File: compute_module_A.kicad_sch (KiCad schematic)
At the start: 15 parts, among them J6 MagJack, J7 Micro_SD_Card_Det, U4 RT9742GGJ5

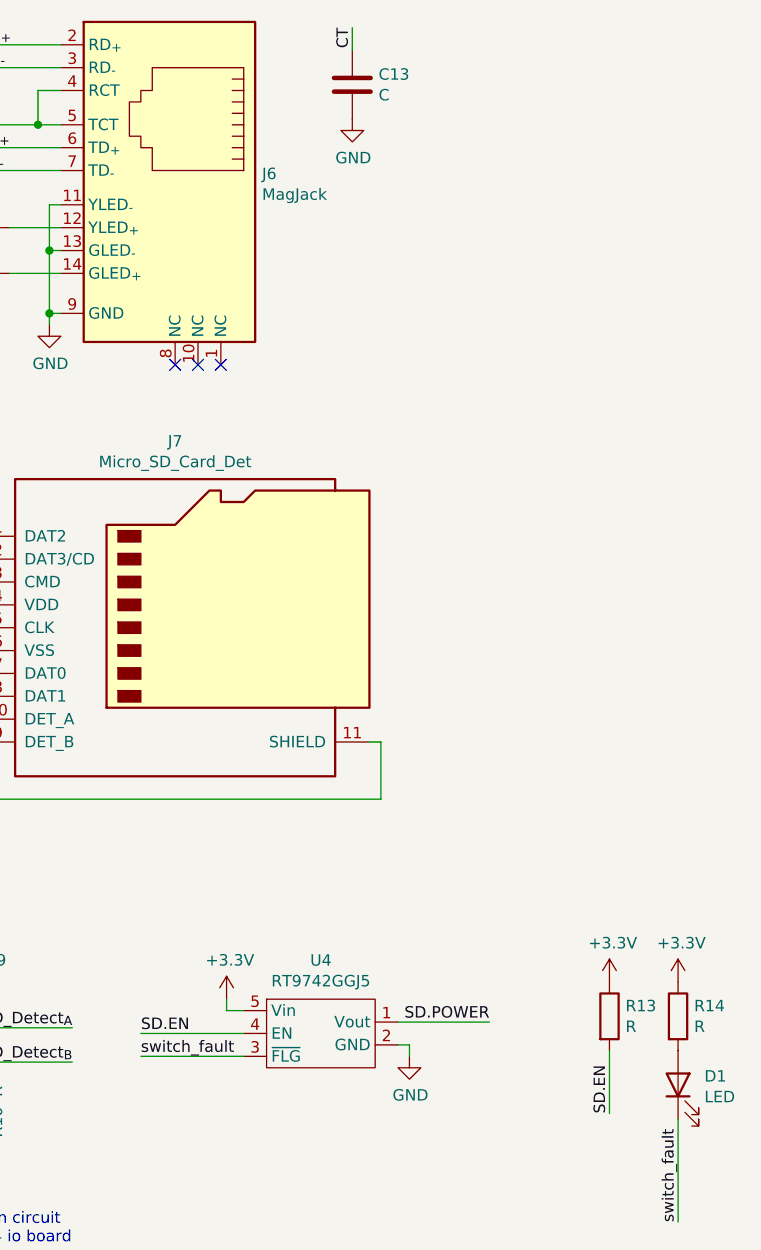
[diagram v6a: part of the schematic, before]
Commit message: footprint assignments
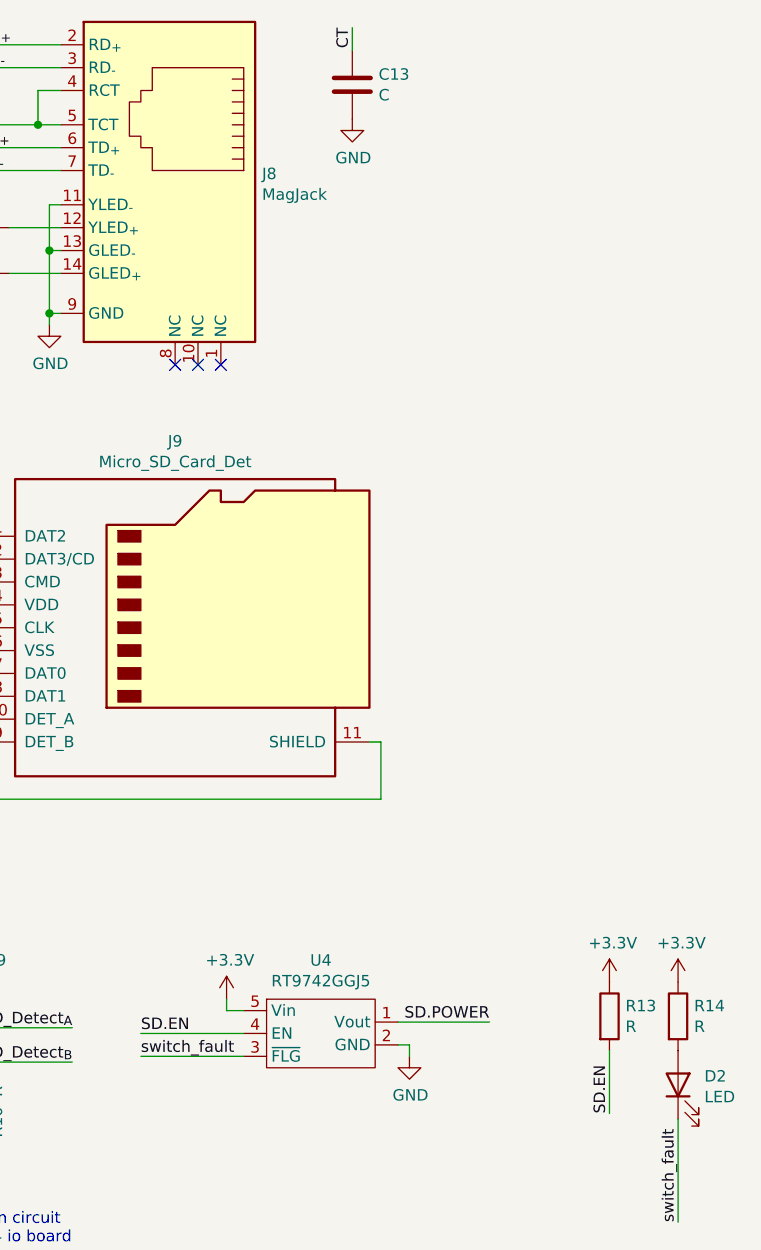
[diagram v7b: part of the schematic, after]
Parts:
- J9: renamed from J7; Vendor Part (none) -> HR1941CT-ND
- renumbered D1 to D2, J6 to J8
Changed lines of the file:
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@@
   (junction (at 184.785 53.975) (diameter 0.9144) (color 0 0 0 0))
   (junction (at 184.785 60.96) (diameter 0.9144) (color 0 0 0 0))
+  (no_connect (at 198.755 66.675))
+  (no_connect (at 94.615 41.91))
   (no_connect (at 33.655 49.53))
+  (no_connect (at 203.835 66.675))
+  (no_connect (at 201.295 66.675))
+  (no_connect (at 33.655 52.07))
+  (no_connect (at 94.615 62.23))
   (no_connect (at 94.615 44.45))
-  (no_connect (at 198.755 66.675))
-  (no_connect (at 94.615 62.23))
-  (no_connect (at 33.655 52.07))
-  (no_connect (at 94.615 41.91))
-  (no_connect (at 201.295 66.675))
-  (no_connect (at 203.835 66.675))
   (wire (pts (xy 20.955 133.35) (xy 33.655 133.35))
     (stroke (width 0) (type solid) (color 0 0 0 0))
@@
   (symbol (lib_id "power:+3.3V") (at 28.575 125.095 0) (unit 1)
     (in_bom yes) (on_board yes)
-    (property "Reference" "#PWR0120" (id 0) (at 28.575 128.905 0)
+    (property "Reference" "#PWR0124" (id 0) (at 28.575 128.905 0)
       (effects (font (size 1.27 1.27)) hide)
     )
@@
   (symbol (lib_id "power:+5V") (at 110.49 133.985 0) (unit 1)
     (in_bom yes) (on_board yes)
-    (property "Reference" "#PWR0121" (id 0) (at 110.49 137.795 0)
+    (property "Reference" "#PWR0126" (id 0) (at 110.49 137.795 0)
       (effects (font (size 1.27 1.27)) hide)
     )
@@
   (symbol (lib_id "power:+3.3V") (at 121.92 180.975 0) (unit 1)
     (in_bom yes) (on_board yes)
-    (property "Reference" "#PWR0127" (id 0) (at 121.92 184.785 0)
+    (property "Reference" "#PWR0131" (id 0) (at 121.92 184.785 0)
       (effects (font (size 1.27 1.27)) hide)
     )
@@
   (symbol (lib_id "power:+3.3V") (at 139.065 180.975 0) (unit 1)
     (in_bom yes) (on_board yes)
-    (property "Reference" "#PWR0124" (id 0) (at 139.065 184.785 0)
+    (property "Reference" "#PWR0129" (id 0) (at 139.065 184.785 0)
       (effects (font (size 1.27 1.27)) hide)
     )
@@
   (symbol (lib_id "power:+3.3V") (at 175.895 130.175 0) (unit 1)
     (in_bom yes) (on_board yes)
-    (property "Reference" "#PWR0130" (id 0) (at 175.895 133.985 0)
+    (property "Reference" "#PWR0133" (id 0) (at 175.895 133.985 0)
       (effects (font (size 1.27 1.27)) hide)
     )
@@
   (symbol (lib_id "power:+3.3V") (at 204.47 137.16 0) (unit 1)
     (in_bom yes) (on_board yes)
-    (property "Reference" "#PWR0132" (id 0) (at 204.47 140.97 0)
+    (property "Reference" "#PWR0137" (id 0) (at 204.47 140.97 0)
       (effects (font (size 1.27 1.27)) hide)
     )
@@
   (symbol (lib_id "power:+3.3V") (at 247.015 135.255 0) (unit 1)
     (in_bom yes) (on_board yes)
-    (property "Reference" "#PWR0135" (id 0) (at 247.015 139.065 0)
+    (property "Reference" "#PWR0139" (id 0) (at 247.015 139.065 0)
       (effects (font (size 1.27 1.27)) hide)
     )
@@
   (symbol (lib_id "power:+3.3V") (at 254.635 135.255 0) (unit 1)
     (in_bom yes) (on_board yes)
-    (property "Reference" "#PWR0134" (id 0) (at 254.635 139.065 0)
+    (property "Reference" "#PWR0138" (id 0) (at 254.635 139.065 0)
       (effects (font (size 1.27 1.27)) hide)
     )
@@
   (symbol (lib_id "power:GND") (at 98.425 171.45 0) (unit 1)
     (in_bom yes) (on_board yes)
-    (property "Reference" "#PWR0126" (id 0) (at 98.425 177.8 0)
+    (property "Reference" "#PWR0125" (id 0) (at 98.425 177.8 0)
       (effects (font (size 1.27 1.27)) hide)
     )
@@
   (symbol (lib_id "power:GND") (at 121.92 188.595 0) (unit 1)
     (in_bom yes) (on_board yes)
-    (property "Reference" "#PWR0125" (id 0) (at 121.92 194.945 0)
+    (property "Reference" "#PWR0130" (id 0) (at 121.92 194.945 0)
       (effects (font (size 1.27 1.27)) hide)
     )
@@
   (symbol (lib_id "power:GND") (at 130.81 188.595 0) (unit 1)
     (in_bom yes) (on_board yes)
-    (property "Reference" "#PWR0122" (id 0) (at 130.81 194.945 0)
+    (property "Reference" "#PWR0128" (id 0) (at 130.81 194.945 0)
       (effects (font (size 1.27 1.27)) hide)
     )
@@
   (symbol (lib_id "power:GND") (at 139.065 188.595 0) (unit 1)
     (in_bom yes) (on_board yes)
-    (property "Reference" "#PWR0123" (id 0) (at 139.065 194.945 0)
+    (property "Reference" "#PWR0127" (id 0) (at 139.065 194.945 0)
       (effects (font (size 1.27 1.27)) hide)
     )
@@
   (symbol (lib_id "power:GND") (at 175.895 116.205 0) (unit 1)
     (in_bom yes) (on_board yes)
-    (property "Reference" "#PWR0131" (id 0) (at 175.895 122.555 0)
+    (property "Reference" "#PWR0132" (id 0) (at 175.895 122.555 0)
       (effects (font (size 1.27 1.27)) hide)
     )
@@
   (symbol (lib_id "power:GND") (at 184.785 62.23 0) (unit 1)
     (in_bom yes) (on_board yes)
-    (property "Reference" "#PWR0128" (id 0) (at 184.785 68.58 0)
+    (property "Reference" "#PWR0134" (id 0) (at 184.785 68.58 0)
       (effects (font (size 1.27 1.27)) hide)
     )
@@
   (symbol (lib_id "power:GND") (at 218.44 39.37 0) (unit 1)
     (in_bom yes) (on_board yes)
-    (property "Reference" "#PWR0129" (id 0) (at 218.44 45.72 0)
+    (property "Reference" "#PWR0135" (id 0) (at 218.44 45.72 0)
       (effects (font (size 1.27 1.27)) hide)
     )
@@
   (symbol (lib_id "power:GND") (at 224.79 143.51 0) (unit 1)
     (in_bom yes) (on_board yes)
-    (property "Reference" "#PWR0133" (id 0) (at 224.79 149.86 0)
+    (property "Reference" "#PWR0136" (id 0) (at 224.79 149.86 0)
       (effects (font (size 1.27 1.27)) hide)
     )
@@
   (symbol (lib_id "Device:LED") (at 254.635 146.685 90) (unit 1)
     (in_bom yes) (on_board yes)
-    (property "Reference" "D1" (id 0) (at 257.5561 145.7261 90)
+    (property "Reference" "D2" (id 0) (at 257.5561 145.7261 90)
       (effects (font (size 1.27 1.27)) (justify right))
     )
@@
   (symbol (lib_id "symbols:MagJack") (at 192.405 41.275 0) (unit 1)
     (in_bom yes) (on_board yes)
-    (property "Reference" "J6" (id 0) (at 208.4071 45.4533 0)
+    (property "Reference" "J8" (id 0) (at 208.4071 45.4533 0)
       (effects (font (size 1.27 1.27)) (justify left))
     )
@@
   (symbol (lib_id "symbols:Micro_SD_Card_Det") (at 200.025 95.885 0) (unit 1)
     (in_bom yes) (on_board yes)
-    (property "Reference" "J7" (id 0) (at 198.755 75.1648 0))
+    (property "Reference" "J9" (id 0) (at 198.755 75.1648 0))
     (property "Value" "Micro_SD_Card_Det" (id 1) (at 198.755 77.4635 0))
     (property "Footprint" "Connector_Card:microSD_HC_Hirose_DM3D-SF" (id 2) (at 252.095 78.105 0)
@@
       (effects (font (size 1.27 1.27)) hide)
     )
+    (property "Vendor Part" "HR1941CT-ND" (id 8) (at 200.025 95.885 0)
+      (effects (font (size 1.27 1.27)) hide)
+    )
